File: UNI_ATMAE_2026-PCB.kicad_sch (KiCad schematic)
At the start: 0 parts

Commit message: Oct-14-26 Initial PCB design
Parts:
- added U1: (no value), Project Footprints:ESP32_DevBoard, symbol Project Symbols:ESP32_DevBoard
- added U2: (no value), Project Footprints:Voltage Buck conv. (DROK), symbol Project Symbols:Voltage_Buck_conv. (DROK)
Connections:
- new net: U1.16 (VIN), U2.1 (VO+)
- new net GND: U1.17 (GND), U1.2 (GND), U2.2 (GND)

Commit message: Oct-14-26
Added basic components to PCB
Updated symbols again
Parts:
- removed U1: (no value), Project Footprints:ESP32_DevBoard, symbol Project Symbols:ESP32_DevBoard
- added ESP32-1: ESP32, Project Footprints:ESP32_DevBoard, symbol Project Symbols:ESP32_DevBoard
- added J1: Power In, Connector_JST:JST_XH_B2B-XH-A_1x02_P2.50mm_Vertical, symbol Connector:Conn_01x02_Socket
- added J2: Motor Driver, Connector_JST:JST_XH_B4B-XH-A_1x04_P2.50mm_Vertical, symbol Connector:Conn_01x04_Socket
- added J3: Out 1, Connector_JST:JST_XH_B4B-XH-A_1x04_P2.50mm_Vertical, symbol Connector:Conn_01x04_Socket
- U2: value (none) -> Buck Converter
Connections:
- net GND: now also ESP32-1.17 (GND), ESP32-1.2 (GND), J1.1 (Pin_1), J2.1 (Pin_1), J3.1 (Pin_1)
- net at U2.1 (VO+): now also ESP32-1.16 (VIN), J2.2 (Pin_2), J3.2 (Pin_2)
- net at U2.3 (VIN+): now also J1.2 (Pin_2)
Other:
- moved on the sheet: U2

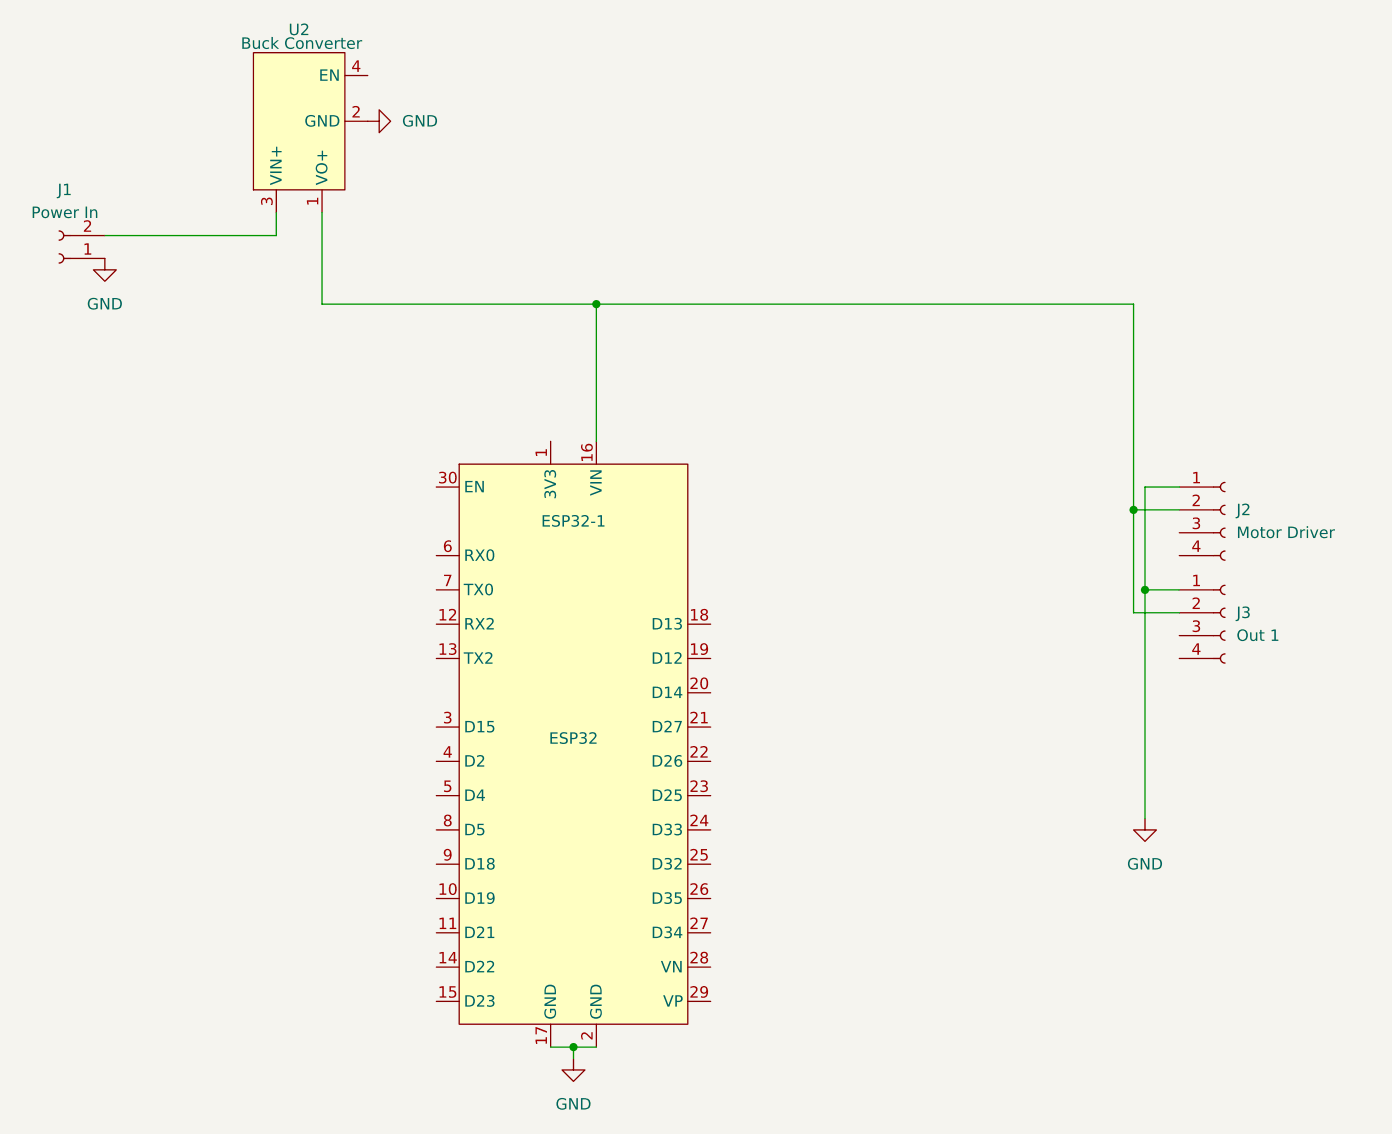
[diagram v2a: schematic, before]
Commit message: Oct-15-26
Added Logic Level shifter symbol/footprint
Updated labels on project schematics to not move when added to project
Basic test PCB design
Added README file
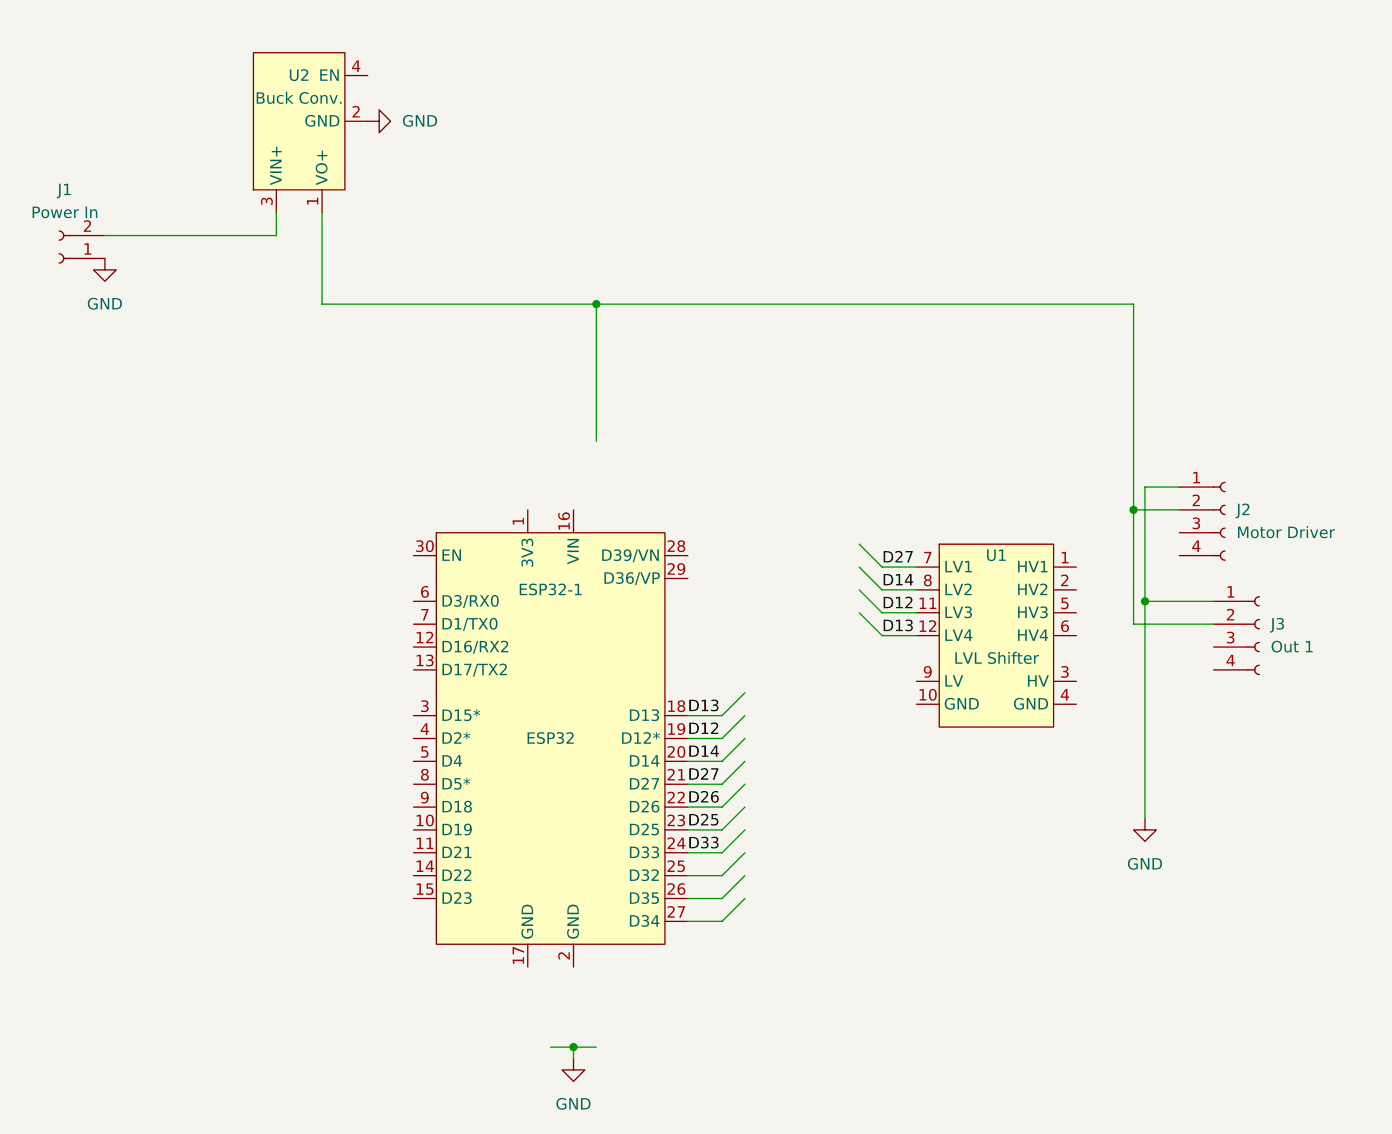
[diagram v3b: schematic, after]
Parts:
- added U1: LVL Shifter, Project Footprints:Logic Level Shifter-4Ch, symbol Project Symbols:Logic_Level_Shifter-4Ch
- U2: value Buck Converter -> Buck Conv.
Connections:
- net GND: no longer ESP32-1.17 (GND), ESP32-1.2 (GND)
- net at J2.2 (Pin_2), J3.2 (Pin_2), U2.1 (VO+): no longer ESP32-1.16 (VIN)
- net D13: now reaches ESP32-1.18 (D13)
- net D13: now also U1.12 (LV4)
- net D12: now reaches ESP32-1.19 (D12*)
- net D12: now also U1.11 (LV3)
- net D14: now reaches ESP32-1.20 (D14)
- net D14: now also U1.8 (LV2)
- net D27: now reaches ESP32-1.21 (D27)
- net D27: now also U1.7 (LV1)
- net D26: now reaches ESP32-1.22 (D26)
- net D25: now reaches ESP32-1.23 (D25)
- net D33: now reaches ESP32-1.24 (D33)
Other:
- moved on the sheet: J3

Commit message: Oct-15-26
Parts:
- added J4: Out 1, Connector_JST:JST_XH_B4B-XH-A_1x04_P2.50mm_Vertical, symbol Connector:Conn_01x04_Socket
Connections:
- net GND: now also U1.10 (GND), U1.4 (GND), J4.1 (Pin_1)
- net 5V: now reaches J1.2 (Pin_2), U2.3 (VIN+)
- net 5V: now also ESP32-1.16 (VIN), J2.2 (Pin_2), J3.2 (Pin_2), U1.3 (HV), J4.2 (Pin_2)
- net 3.3V: now reaches ESP32-1.1 (3V3)
- net 3.3V: now also U1.9 (LV), U2.1 (VO+)
- net at ESP32-1.12 (D16/RX2): now also J2.4 (Pin_4)
- net at ESP32-1.13 (D17/TX2): now also J2.3 (Pin_3)
- net at U1.1 (HV1): now also J3.4 (Pin_4)
- net at U1.2 (HV2): now also J3.3 (Pin_3)
- net at U1.5 (HV3): now also J4.4 (Pin_4)
- net at U1.6 (HV4): now also J4.3 (Pin_3)
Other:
- moved on the sheet: J1, J2, J3, U2

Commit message: Oct-15-26
Connected generic JST-XH connectors for 8 I/O pins through level shifters
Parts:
- added J5: Out 3, Connector_JST:JST_XH_B4B-XH-A_1x04_P2.50mm_Vertical, symbol Connector:Conn_01x04_Socket
- added J6: Out 4, Connector_JST:JST_XH_B4B-XH-A_1x04_P2.50mm_Vertical, symbol Connector:Conn_01x04_Socket
- added U3: LVL Shifter, Project Footprints:Logic Level Shifter-4Ch, symbol Project Symbols:Logic_Level_Shifter-4Ch
- J4: value Out 1 -> Out 2
- renumbered U2 to U1, U1 to U2
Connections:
- net 3.3V: now also U3.9 (LV)
- net 5V: now also J5.2 (Pin_2), J6.2 (Pin_2), U3.3 (HV)
- net D25: now also U3.11 (LV3)
- net D26: now also U3.12 (LV4)
- net D33: now also U3.8 (LV2)
- net GND: now also J5.1 (Pin_1), J6.1 (Pin_1), U3.10 (GND), U3.4 (GND)
- net D32: now reaches ESP32-1.25 (D32)
- net D32: now also U3.7 (LV1)
- new net: J5.3 (Pin_3), U3.2 (HV2)
- new net: J5.4 (Pin_4), U3.1 (HV1)
- new net: J6.4 (Pin_4), U3.5 (HV3)
- new net: J6.3 (Pin_3), U3.6 (HV4)
